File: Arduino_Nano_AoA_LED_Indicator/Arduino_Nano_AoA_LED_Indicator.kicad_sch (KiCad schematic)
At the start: 20 parts

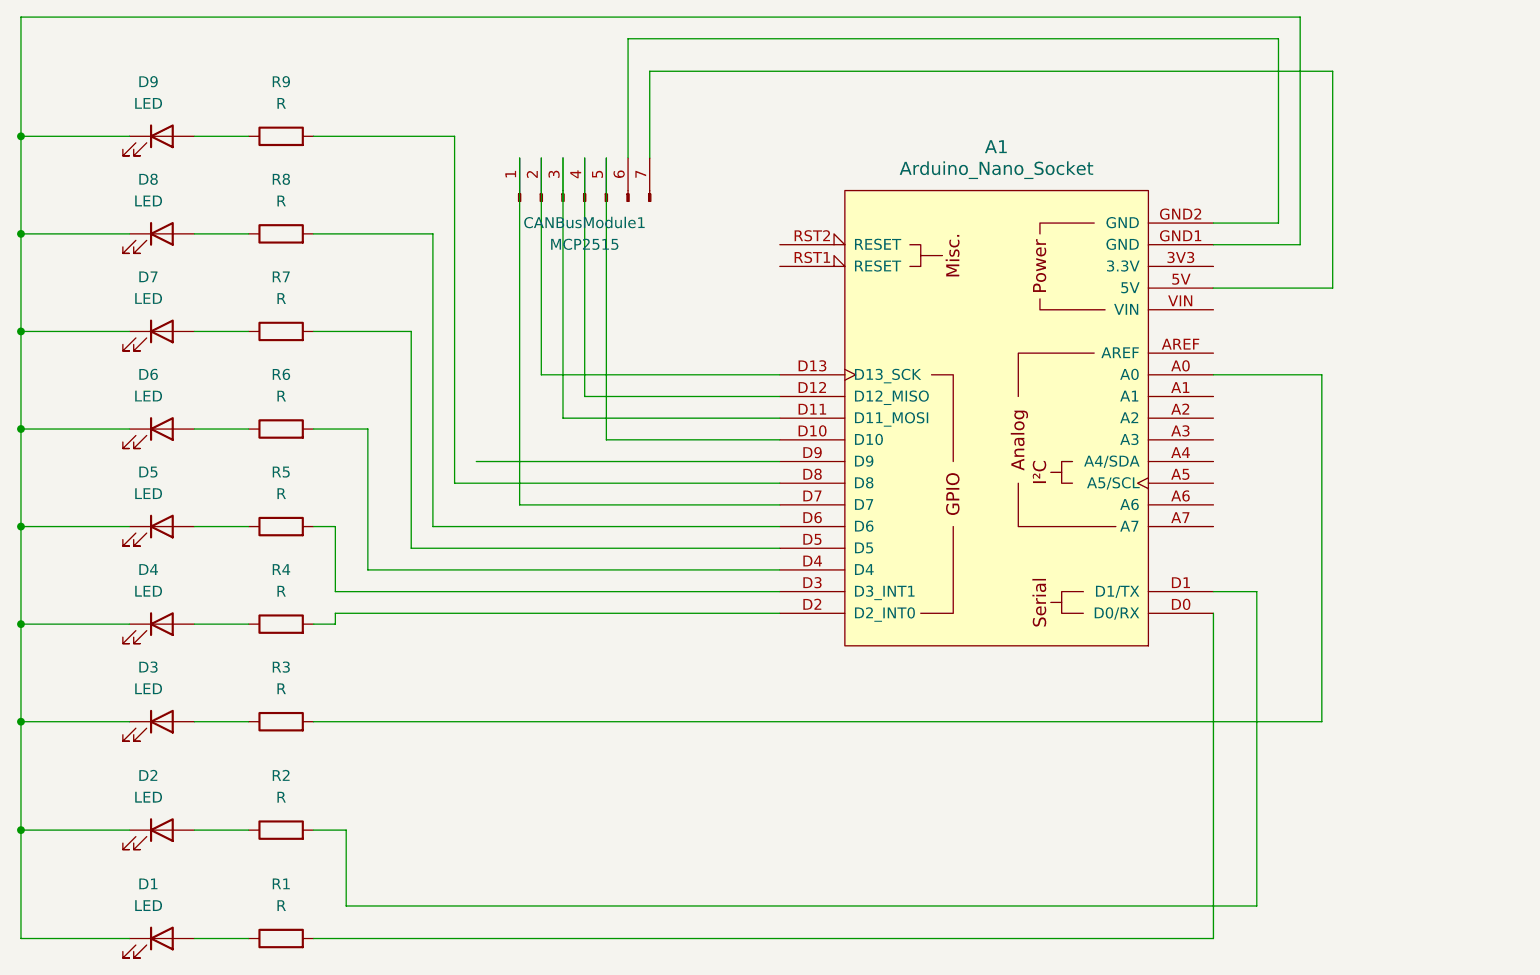
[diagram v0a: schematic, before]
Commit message: Split the AOA LED project into two projects - one for the LEDs and one for the Nano board and the MCP2515 CAN board.
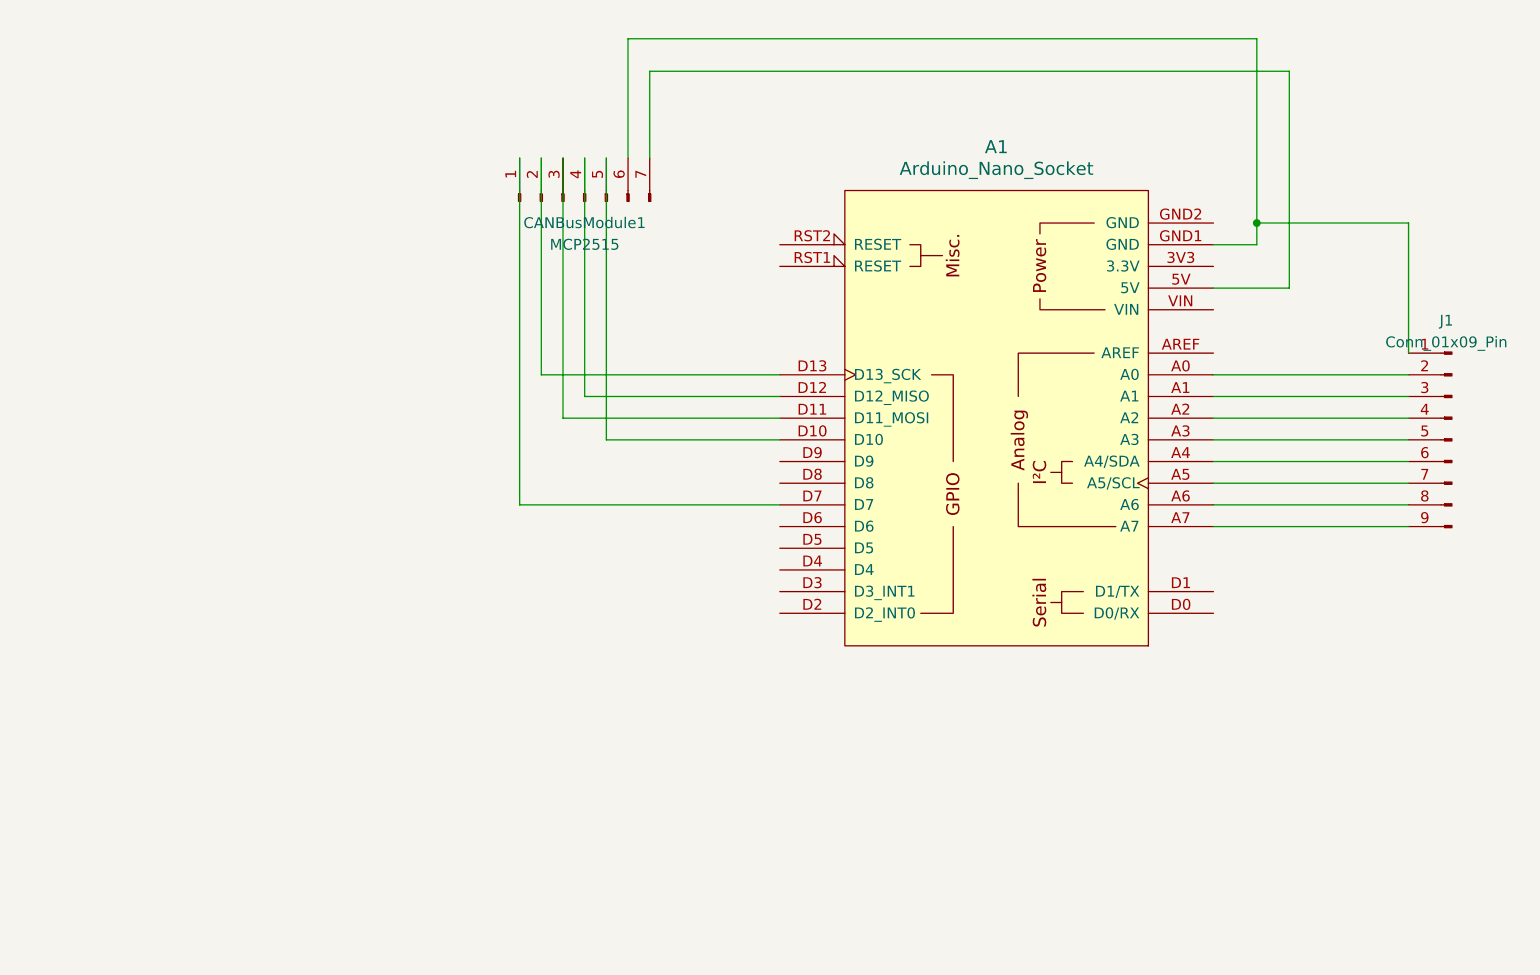
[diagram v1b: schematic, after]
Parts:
- removed D1, D2, D3, D4, D5, D6, D7, D8, D9: LED, LED_SMD:LED_Yuji_5730, symbol Device:LED
- removed R1, R2, R3, R4, R5, R6, R7, R8, R9: R, Resistor_SMD:R_1206_3216Metric, symbol Device:R
- added J1: Conn_01x09_Pin, Connector_PinHeader_2.54mm:PinHeader_1x09_P2.54mm_Horizontal, symbol Connector:Conn_01x09_Pin
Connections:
- net at A1.GND1 (GND): now also CANBusModule1.6 (Pin_6), J1.1 (Pin_1)
- net at A1.A0: now also J1.2 (Pin_2)
- net at A1.A1: now also J1.3 (Pin_3)
- net at A1.A2: now also J1.4 (Pin_4)
- net at A1.A3: now also J1.5 (Pin_5)
- net at A1.A4 (A4/SDA): now also J1.6 (Pin_6)
- net at A1.A5 (A5/SCL): now also J1.7 (Pin_7)
- net at A1.A6: now also J1.8 (Pin_8)
- net at A1.A7: now also J1.9 (Pin_9)
- net at A1.GND2 (GND): no longer CANBusModule1.6 (Pin_6)
